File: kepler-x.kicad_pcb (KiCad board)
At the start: 2 copper layers, 140.5 x 150 mm, 7 parts, among them U1 Bus-X68000-ext, U2 74LVT162245, U3 74LVT162245, U4 74LVT162245, U5 CS8421-CZZ, U6 WM8804GEDS/RV

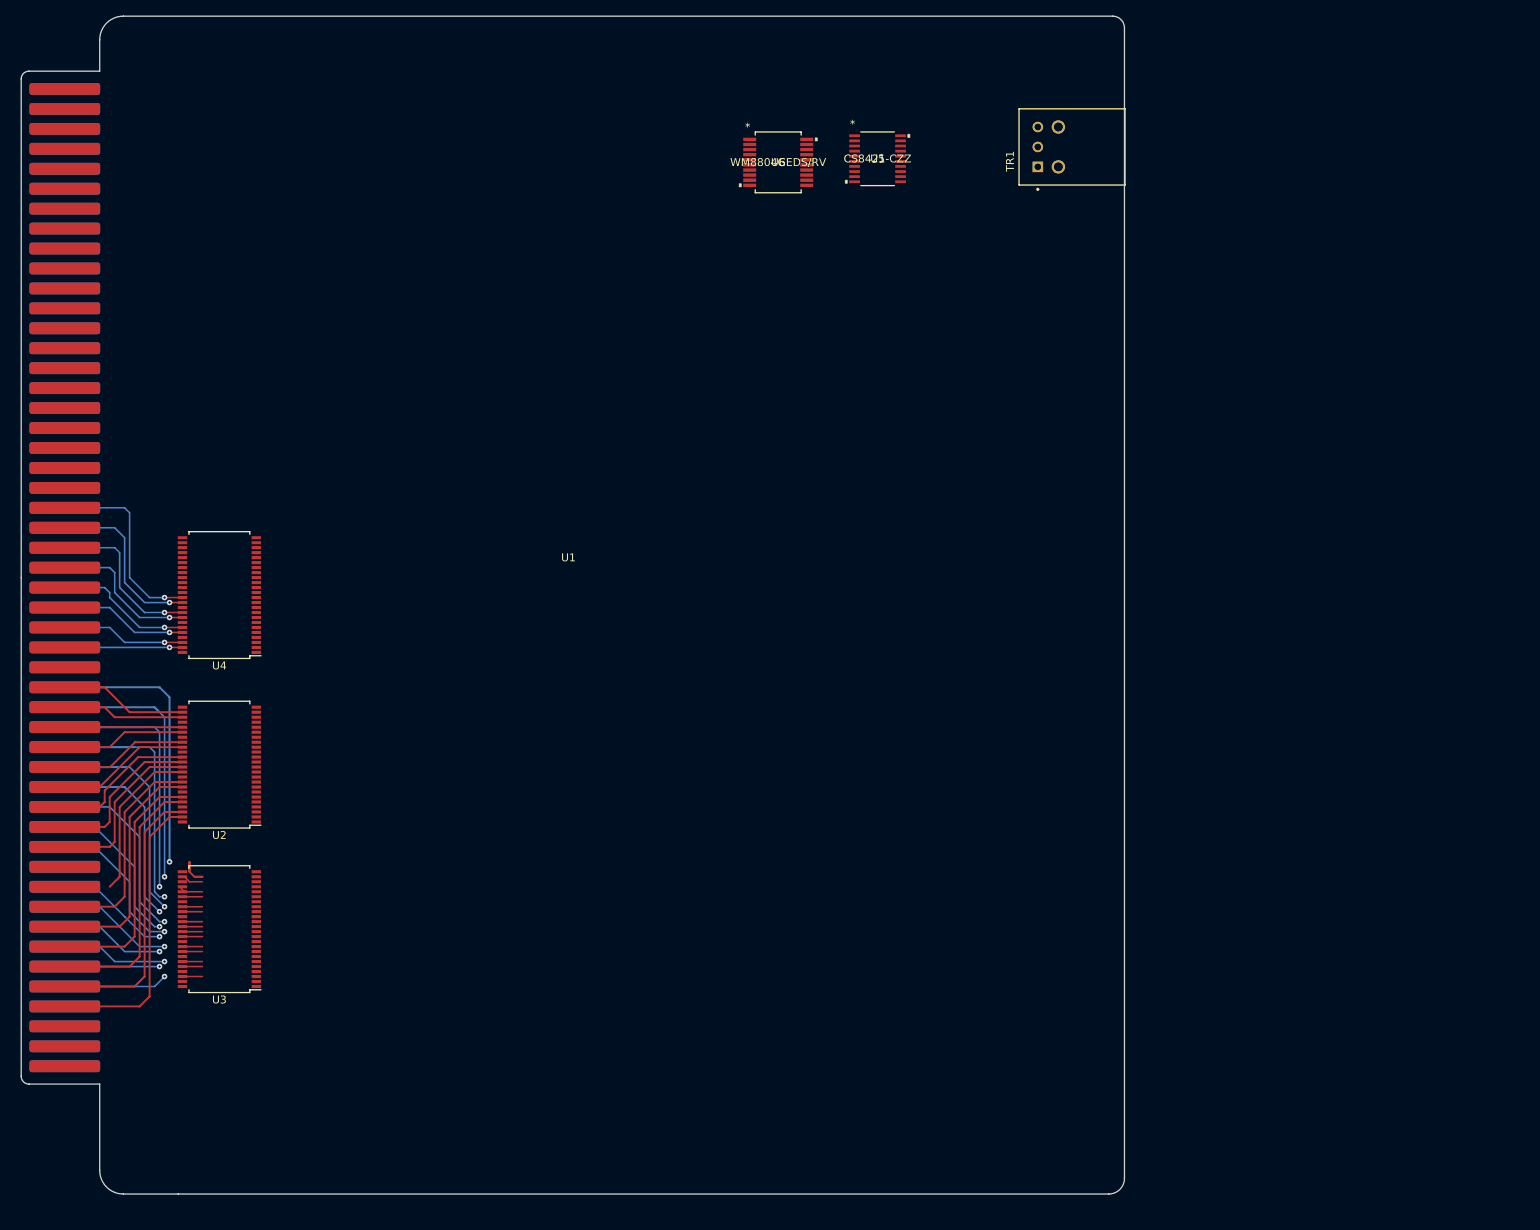
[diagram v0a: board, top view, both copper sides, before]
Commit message: Add fooprints
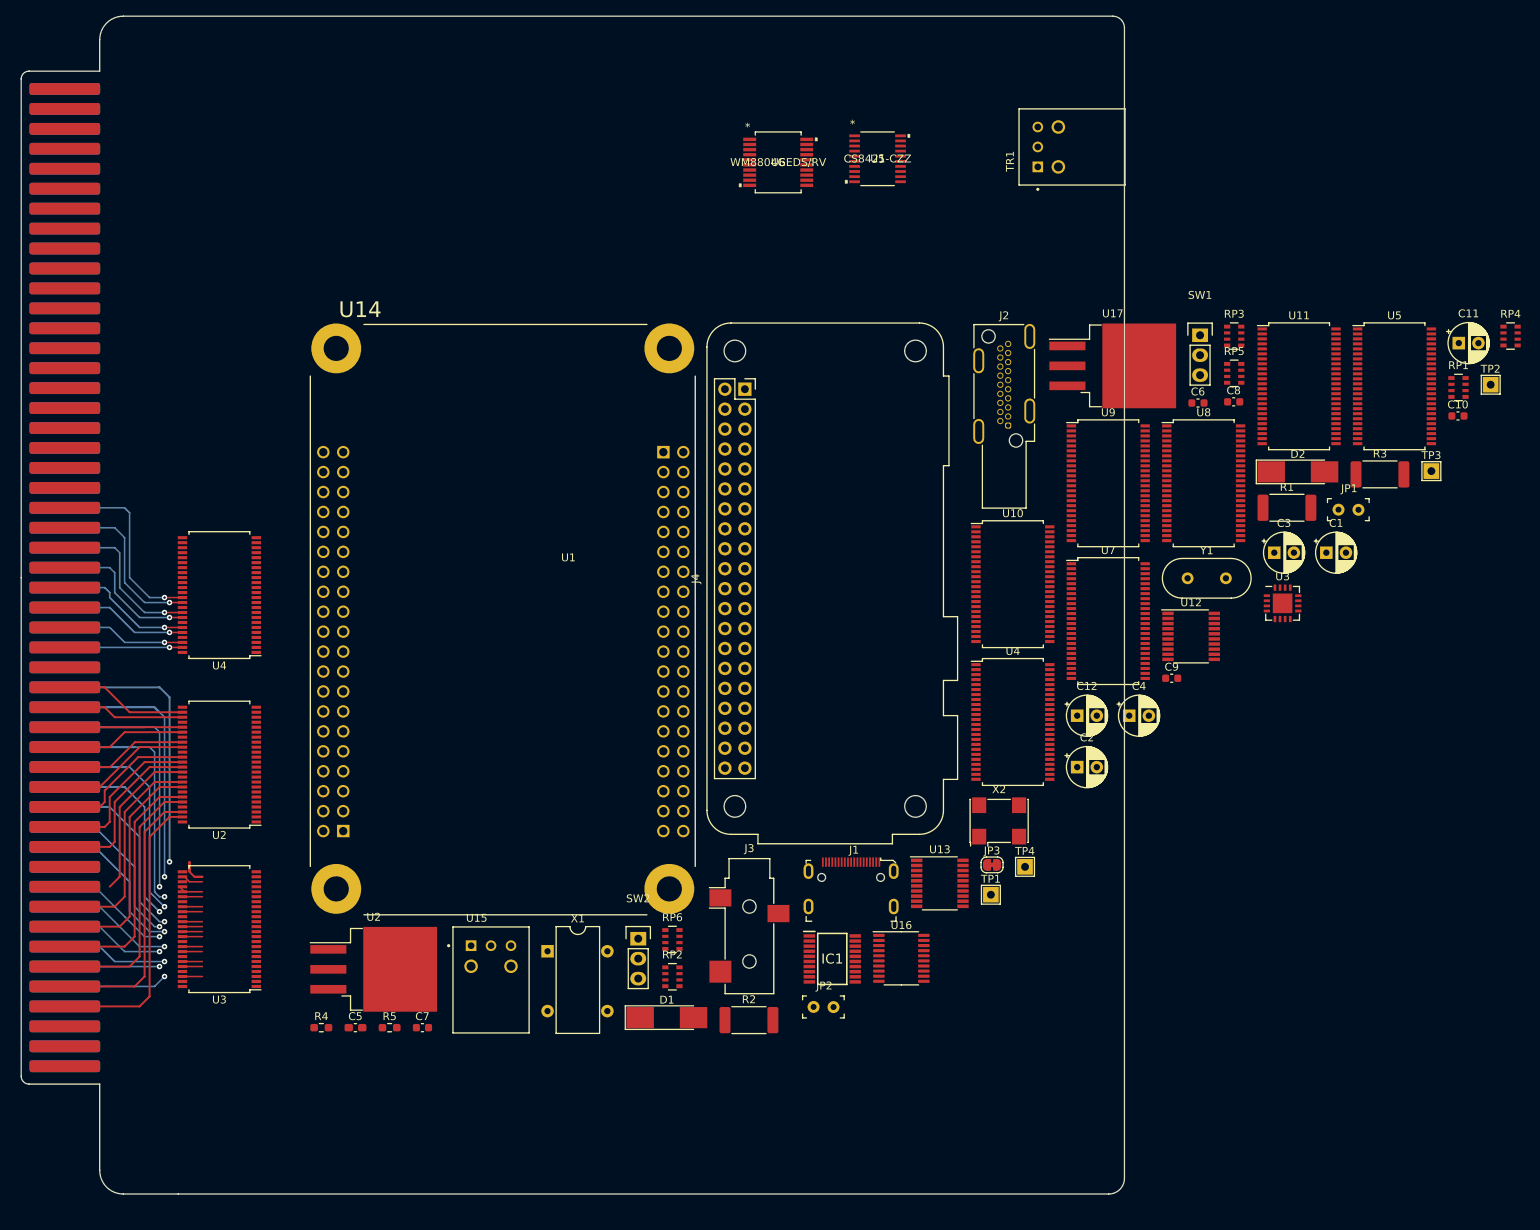
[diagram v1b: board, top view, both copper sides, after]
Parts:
- added C1: 10uF, Capacitor_THT:CP_Radial_D5.0mm_P2.50mm, F.Cu at (196.8, 95.9)
- added C10: 0.1uF, Capacitor_SMD:C_0603_1608Metric, F.Cu at (213.6, 78.5)
- added C11: 10uF, Capacitor_THT:CP_Radial_D5.0mm_P2.50mm, F.Cu at (213.7, 69.2)
- added C12: 100uF, Capacitor_THT:CP_Radial_D5.0mm_P2.50mm, F.Cu at (165.1, 116.6)
- added C2: 100uF, Capacitor_THT:CP_Radial_D5.0mm_P2.50mm, F.Cu at (165.1, 123.2)
- added C3: 1uF, Capacitor_THT:CP_Radial_D5.0mm_P2.50mm, F.Cu at (190.2, 95.9)
- added C4: 15pF, Capacitor_THT:CP_Radial_D5.0mm_P2.50mm, F.Cu at (171.8, 116.6)
- added C5: 15pF, Capacitor_SMD:C_0603_1608Metric_Pad1.08x0.95mm_HandSolder, F.Cu at (73.2, 156.4)
- added C6: 0.1uF, Capacitor_SMD:C_0603_1608Metric, F.Cu at (180.5, 76.8)
- added C7: 0.1uF, Capacitor_SMD:C_0603_1608Metric, F.Cu at (81.7, 156.4)
- added C8: 2.2uF, Capacitor_SMD:C_0603_1608Metric, F.Cu at (185.1, 76.7)
- added C9: 2.2uF, Capacitor_SMD:C_0603_1608Metric, F.Cu at (177.2, 111.9)
- added D1: D_Schottky_Small, Diode_SMD:D_MELF_Handsoldering, F.Cu at (112.9, 155.1)
- added D2: D_Schottky_Small, Diode_SMD:D_MELF_Handsoldering, F.Cu at (193.2, 85.6)
- added IC1: SLG46826G, x68000-ext:SOP65P640X120-20N, F.Cu at (133.9, 147.6)
- added J1: HDMI_C_1.3, digikey-footprints:HDMI_Mini_Female_2001-1-2-21-00-BK, F.Cu at (136.3, 135.3)
- added J2: HDMI_A, Connector_HDMI:HDMI_A_Kycon_KDMIX-SL1-NS-WS-B15_VerticalRightAngle, F.Cu at (156.3, 79.7)
- added J3: Jack_3.5mm_3pin, Connector_Audio:Jack_3.5mm_CUI_SJ-3523-SMT_Horizontal, F.Cu at (123.4, 143.4)
- added J4: RasPI_IO_Header_B+, Module:Raspberry_Pi_Zero_Socketed_THT_FaceDown_MountingHoles, F.Cu at (122.8, 75.1)
- added JP1: Jumper_NC_Small, digikey-footprints:PinHeader_1x2_P2.54mm, F.Cu at (198.4, 90.4)
- added JP2: Jumper_NC_Small, digikey-footprints:PinHeader_1x2_P2.54mm, F.Cu at (131.6, 153.7)
- added JP3: Jumper_NC_Small, Jumper:SolderJumper-2_P1.3mm_Bridged_RoundedPad1.0x1.5mm, F.Cu at (154.3, 135.6)
- added R1: R100 (0.1Ω), Resistor_SMD:R_2512_6332Metric_Pad1.40x3.35mm_HandSolder, F.Cu at (191.8, 90.2)
- added R2: R100 (0.1Ω), Resistor_SMD:R_2512_6332Metric_Pad1.40x3.35mm_HandSolder, F.Cu at (123.3, 155.4)
- added R3: R100 (0.1Ω), Resistor_SMD:R_2512_6332Metric_Pad1.40x3.35mm_HandSolder, F.Cu at (203.7, 85.9)
- added R4: R_US, Resistor_SMD:R_0603_1608Metric_Pad0.98x0.95mm_HandSolder, F.Cu at (68.9, 156.4)
- added R5: R_US, Resistor_SMD:R_0603_1608Metric_Pad0.98x0.95mm_HandSolder, F.Cu at (77.6, 156.4)
- added RP1: R_PACK4, Resistor_SMD:R_Array_Convex_4x0603, F.Cu at (213.7, 74.8)
- added RP2: R_PACK4, Resistor_SMD:R_Array_Convex_4x0603, F.Cu at (113.6, 149.9)
- added RP3: R_PACK4, Resistor_SMD:R_Array_Convex_4x0603, F.Cu at (185.1, 68.3)
- added RP4: R_PACK4, Resistor_SMD:R_Array_Convex_4x0603, F.Cu at (220.3, 68.3)
- added RP5: 270, Resistor_SMD:R_Array_Convex_4x0603, F.Cu at (185.1, 73.0)
- added RP6: 270, Resistor_SMD:R_Array_Convex_4x0603, F.Cu at (113.6, 145.1)
- added SW1: SWITCH_INV, Pin_Headers:Pin_Header_Straight_1x03, F.Cu at (180.8, 68.2)
- added SW2: SWITCH_INV, Pin_Headers:Pin_Header_Straight_1x03, F.Cu at (109.2, 145.0)
- added TP1: TestPoint, TestPoint:TestPoint_THTPad_2.0x2.0mm_Drill1.0mm, F.Cu at (154.1, 139.4)
- added TP2: TestPoint, TestPoint:TestPoint_THTPad_2.0x2.0mm_Drill1.0mm, F.Cu at (217.8, 74.5)
- added TP3: TestPoint, TestPoint:TestPoint_THTPad_2.0x2.0mm_Drill1.0mm, F.Cu at (210.2, 85.5)
- added TP4: TestPoint, TestPoint:TestPoint_THTPad_2.0x2.0mm_Drill1.0mm, F.Cu at (158.5, 135.9)
- added U10: 74AHC16374, Housings_SSOP:SSOP-48_7.5x15.9mm_Pitch0.635mm, F.Cu at (156.9, 99.9)
- added U11: 74LVTH162245, Housings_SSOP:SSOP-48_7.5x15.9mm_Pitch0.635mm, F.Cu at (193.4, 74.7)
- added U12: TC7MPB9307F, Housings_SSOP:TSSOP-20_4.4x6.5mm_Pitch0.65mm, F.Cu at (179.6, 106.5)
- added U13: TC7MPB9307F, Housings_SSOP:TSSOP-20_4.4x6.5mm_Pitch0.65mm, F.Cu at (147.6, 138.0)
- added U14: P0082(DE0-NANO), x68000-ext:MODULE_P0082_BOTTOMMOUNT, F.Cu at (92.0, 104.4)
- added U15: PLR135-T10, x68000-ext:XDCR_PLT133_T10W, F.Cu at (90.5, 148.6)
- added U16: PCM5102, Package_SO:TSSOP-20_4.4x6.5mm_P0.65mm, F.Cu at (142.7, 147.5)
- added U17: LT1117-3.3, Package_TO_SOT_SMD:TO-263-3_TabPin2, F.Cu at (169.7, 72.1)
- added U2: LT1117-3.3, Package_TO_SOT_SMD:TO-263-3_TabPin2, F.Cu at (75.5, 148.9)
- added U3: INA3221, Housings_DFN_QFN:QFN-16-1EP_4x4mm_Pitch0.65mm, F.Cu at (191.3, 102.3)
- added U4: 74AHC16374, Housings_SSOP:SSOP-48_7.5x15.9mm_Pitch0.635mm, F.Cu at (156.9, 117.4)
- added U5: 74AHC16374, Housings_SSOP:SSOP-48_7.5x15.9mm_Pitch0.635mm, F.Cu at (205.5, 74.7)
- added U7: 74AHC16374, Housings_SSOP:SSOP-48_7.5x15.9mm_Pitch0.635mm, F.Cu at (169.1, 104.6)
- added U8: 74AHC16374, Housings_SSOP:SSOP-48_7.5x15.9mm_Pitch0.635mm, F.Cu at (181.2, 87.0)
- added U9: 74AHC16374, Housings_SSOP:SSOP-48_7.5x15.9mm_Pitch0.635mm, F.Cu at (169.1, 87.0)
- added X1: SG-8002DC(24.576MHz), Oscillator:Oscillator_SeikoEpson_SG-8002DC, F.Cu at (97.7, 146.6)
- added X2: ASV-xxxMHz, Oscillator:Oscillator_SMD_Abracon_ASV-4Pin_7.0x5.1mm, F.Cu at (155.2, 130.0)
- added Y1: 12MHz, Crystal:Crystal_HC49-U_Vertical, F.Cu at (179.2, 99.1)
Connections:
- TR1 pad 1: unconnected-(TR1-Pad1) -> Net-(TR1-Pad1)
- TR1 pad 2: unconnected-(TR1-Pad2) -> VCC
- TR1 pad 3: unconnected-(TR1-Pad3) -> GND
- U1 pad A22: unconnected-(U1-PadA22) -> Net-(U1-PadA22)
- U1 pad A23: unconnected-(U1-PadA23) -> Net-(U1-PadA22)
- U1 pad A24: unconnected-(U1-PadA24) -> /ExFC0
- U1 pad A25: unconnected-(U1-PadA25) -> /ExFC1
- U1 pad A26: unconnected-(U1-PadA26) -> /ExFC2
- U1 pad A27: unconnected-(U1-PadA27) -> /ExAS
- U1 pad A28: unconnected-(U1-PadA28) -> /ExLDS
- U1 pad A29: unconnected-(U1-PadA29) -> /ExUDS
- U1 pad A30: unconnected-(U1-PadA30) -> /ExRW
- U1 pad A32: unconnected-(U1-PadA32) -> -12V
- U1 pad A33: unconnected-(U1-PadA33) -> -12V
- U1 pad A36: unconnected-(U1-PadA36) -> /ExDTACK
- U1 pad A37: unconnected-(U1-PadA37) -> /ExEXRESET
- U1 pad A40: unconnected-(U1-PadA40) -> /ExEXPWON
- U1 pad A42: unconnected-(U1-PadA42) -> Net-(U1-PadA42)
- U1 pad A43: unconnected-(U1-PadA43) -> Net-(U1-PadA42)
- U1 pad A49: VCC -> Net-(U1-PadA49)
- U1 pad A50: VCC -> Net-(U1-PadA49)
- U1 pad B2: unconnected-(U1-PadB2) -> /ExCLK10M
- U1 pad B30: unconnected-(U1-PadB30) -> /ExIDDIR
- U1 pad B32: unconnected-(U1-PadB32) -> /ExHSYNC
- U1 pad B33: unconnected-(U1-PadB33) -> /ExVSYNC
- U1 pad B34: unconnected-(U1-PadB34) -> /ExDONE
- U1 pad B35: unconnected-(U1-PadB35) -> /ExDTC
- U1 pad B36: unconnected-(U1-PadB36) -> /ExEXREQ
- U1 pad B37: unconnected-(U1-PadB37) -> /ExEXACK
- U1 pad B38: unconnected-(U1-PadB38) -> /ExEXPCL
- U1 pad B39: unconnected-(U1-PadB39) -> /ExEXOWN
- U1 pad B42: unconnected-(U1-PadB42) -> /ExIRQ2
- U1 pad B43: unconnected-(U1-PadB43) -> /ExIRQ4
- U1 pad B44: unconnected-(U1-PadB44) -> /ExIACK2
- U1 pad B45: unconnected-(U1-PadB45) -> /ExIACK4
- U1 pad B46: unconnected-(U1-PadB46) -> /ExBR
- U1 pad B47: unconnected-(U1-PadB47) -> /ExBG
- U6 pad 10: unconnected-(U6-Pad10) -> Net-(C4-Pad1)
- U6 pad 11: unconnected-(U6-Pad11) -> Net-(C5-Pad1)
- U6 pad 12: unconnected-(U6-Pad12) -> /I2S_DATA_IN
- U6 pad 13: unconnected-(U6-Pad13) -> /I2S_DATA
- U6 pad 14: unconnected-(U6-Pad14) -> /I2S_BCLK
- U6 pad 15: unconnected-(U6-Pad15) -> /I2S_LRCK
- U6 pad 16: unconnected-(U6-Pad16) -> /I2S_MCLK
- U6 pad 17: unconnected-(U6-Pad17) -> Net-(TR1-Pad1)
- U6 pad 18: unconnected-(U6-Pad18) -> GND
- U6 pad 19: unconnected-(U6-Pad19) -> +3V3
- U6 pad 20: unconnected-(U6-Pad20) -> Net-(U15-Pad3)
- U6 pad 7: unconnected-(U6-Pad7) -> +3V3
- U6 pad 8: unconnected-(U6-Pad8) -> GND
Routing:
- net /ExAB15: track 45.0 -> 42.5 mm
- net /ExAB14: track 37.0 -> 39.5 mm

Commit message: Today's version
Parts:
- removed J2: HDMI_A, Connector_HDMI:HDMI_A_Kycon_KDMIX-SL1-NS-WS-B15_VerticalRightAngle
- removed the U2 at (55.9, 122.9)
- removed the U3 at (191.3, 102.3)
- removed the U4 at (156.9, 117.4)
- removed the U5 at (205.5, 74.7)
- added H1: MountingHole, MountingHole:MountingHole_3.7mm, F.Cu at (166.0, 173.0)
- added H2: MountingHole, MountingHole:MountingHole_3.7mm, F.Cu at (166.0, 37.0)
- added H3: MountingHole, MountingHole:MountingHole_2.7mm_M2.5, F.Cu at (152.5, 174.0)
- added H4: MountingHole, MountingHole:MountingHole_2.7mm_M2.5, F.Cu at (152.5, 108.0)
- added J5: Jack_3.5mm_3pin, Connector_Audio:Jack_3.5mm_Switronic_ST-005-G_horizontal, F.Cu at (164.5, 97.8)
- added J6: Jack_3.5mm_3pin, Connector_Audio:Jack_3.5mm_Switronic_ST-005-G_horizontal, F.Cu at (164.5, 107.3)
- C10, C6: footprint Capacitor_SMD:C_0603_1608Metric -> Capacitor_SMD:C_0603_1608Metric_Pad1.08x0.95mm_HandSolder
- C3, C4: footprint Capacitor_THT:CP_Radial_D5.0mm_P2.50mm -> Capacitor_SMD:C_0603_1608Metric_Pad1.08x0.95mm_HandSolder
- C7, C8, C9: footprint Capacitor_SMD:C_0603_1608Metric -> Capacitor_SMD:C_0603_1608Metric_Pad1.08x0.95mm_HandSolder; moved to B.Cu
- J3: footprint Connector_Audio:Jack_3.5mm_CUI_SJ-3523-SMT_Horizontal -> Connector_Audio:Jack_3.5mm_Switronic_ST-005-G_horizontal
- R1, R2, R3, U10, U11, U16, U17, U2, U8, U9, X2: moved to B.Cu
- U3: value 74LVT162245 -> INA3221; footprint Housings_SSOP:SSOP-48_7.5x15.9mm_Pitch0.635mm -> Housings_DFN_QFN:QFN-16-1EP_4x4mm_Pitch0.65mm; moved to B.Cu
- U4: value 74LVT162245 -> 74AHC16374
- U5: value CS8421-CZZ -> 74AHC16374; footprint x68000-ext:CS8421-CZZ -> Housings_SSOP:SSOP-48_7.5x15.9mm_Pitch0.635mm
- moved RP4 165.7 mm to (55.2, 82.5)
- moved R3 158.8 mm to (52.1, 38.7), turned to 180 degrees
- moved RP1 158.6 mm to (55.2, 67.3)
- moved R1 150.5 mm to (52.1, 34.3), turned to 180 degrees
- moved C1 146.0 mm to (57.8, 51.4), turned to 90 degrees
- moved U11 143.2 mm to (50.2, 73.7)
- moved SW1 136.8 mm to (44.4, 57.1), turned to 90 degrees
- moved U12 136.6 mm to (48.3, 69.2), turned to 180 degrees
- moved R2 132.9 mm to (52.1, 43.2), turned to 180 degrees
- moved RP3 129.9 mm to (55.2, 71.1)
- moved R4 127.0 mm to (158.1, 66.0), turned to 180 degrees
- moved C2 126.8 mm to (56.5, 57.8)
- moved U8 125.0 mm to (57.8, 106.7)
- moved C7 121.4 mm to (130.2, 45.1), turned to 90 degrees
- moved R5 119.6 mm to (158.1, 67.9), turned to 180 degrees
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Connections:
- R1 pad 1: Net-(U1-PadA49) -> Net-(R1-Pad1)
- R2 pad 1: Net-(U1-PadA22) -> Net-(R2-Pad1)
- R3 pad 1: Net-(U1-PadA42) -> Net-(R3-Pad1)
- R3 pad 2: Net-(TP1-Pad1) -> Net-(R3-Pad2)
- TP1 pad 1: Net-(TP1-Pad1) -> Net-(R3-Pad2)
- U1 pad A22: Net-(U1-PadA22) -> Net-(R2-Pad1)
- U1 pad A23: Net-(U1-PadA22) -> Net-(R2-Pad1)
- U1 pad A42: Net-(U1-PadA42) -> Net-(R3-Pad1)
- U1 pad A43: Net-(U1-PadA42) -> Net-(R3-Pad1)
- U1 pad A49: Net-(U1-PadA49) -> Net-(R1-Pad1)
- U1 pad A50: Net-(U1-PadA49) -> Net-(R1-Pad1)
- U10 pad 11: /ExDB9 -> /ExDB6
- U10 pad 12: /ExDB8 -> /ExDB7
- U10 pad 13: /ExDB7 -> /ExDB8
- U10 pad 14: /ExDB6 -> /ExDB9
- U10 pad 16: /ExDB5 -> /ExDB10
- U10 pad 17: /ExDB4 -> /ExDB11
- U10 pad 19: /ExDB3 -> /ExDB12
- U10 pad 2: /ExDB15 -> /ExDB0
- U10 pad 20: /ExDB2 -> /ExDB13
- U10 pad 22: /ExDB1 -> /ExDB14
- U10 pad 23: /ExDB0 -> /ExDB15
- U10 pad 26: /iSB0 -> /iSB15
- U10 pad 27: /iSB1 -> /iSB14
- U10 pad 29: /iSB2 -> /iSB13
- U10 pad 3: /ExDB14 -> /ExDB1
- U10 pad 30: /iSB3 -> /iSB12
- U10 pad 32: /iSB4 -> /iSB11
- U10 pad 33: /iSB5 -> /iSB10
- U10 pad 35: /iSB6 -> /iSB9
- U10 pad 36: /iSB7 -> /iSB8
- U10 pad 37: /iSB8 -> /iSB7
- U10 pad 38: /iSB9 -> /iSB6
- U10 pad 40: /iSB10 -> /iSB5
- U10 pad 41: /iSB11 -> /iSB4
- U10 pad 43: /iSB12 -> /iSB3
- U10 pad 44: /iSB13 -> /iSB2
- U10 pad 46: /iSB14 -> /iSB1
- U10 pad 47: /iSB15 -> /iSB0
- U10 pad 5: /ExDB13 -> /ExDB2
- U10 pad 6: /ExDB12 -> /ExDB3
- U10 pad 8: /ExDB11 -> /ExDB4
- U10 pad 9: /ExDB10 -> /ExDB5
- U3 pad 1: unconnected-(U3-Pad1) -> Net-(R3-Pad2)
- U3 pad 11: unconnected-(U3-Pad11) -> VCC
- U3 pad 12: unconnected-(U3-Pad12) -> Net-(R1-Pad1)
- U3 pad 14: unconnected-(U3-Pad14) -> +12V
- U3 pad 15: unconnected-(U3-Pad15) -> Net-(R2-Pad1)
- U3 pad 17: unconnected-(U3-Pad17) -> (no net)
- U3 pad 2: unconnected-(U3-Pad2) -> Net-(R3-Pad1)
- U3 pad 3: unconnected-(U3-Pad3) -> GND
- U3 pad 4: unconnected-(U3-Pad4) -> VCC
- U4 pad 1: unconnected-(U4-Pad1) -> /iB_AI_OE_U
- U4 pad 10: unconnected-(U4-Pad10) -> GND
- U4 pad 11: unconnected-(U4-Pad11) -> /iSB6
- U4 pad 12: unconnected-(U4-Pad12) -> /iSB7
- U4 pad 13: unconnected-(U4-Pad13) -> /iSB8
- U4 pad 14: unconnected-(U4-Pad14) -> /iSB9
- U4 pad 15: unconnected-(U4-Pad15) -> GND
- U4 pad 16: unconnected-(U4-Pad16) -> /iSB10
- U4 pad 17: unconnected-(U4-Pad17) -> /iSB11
- U4 pad 19: unconnected-(U4-Pad19) -> /iSB12
- U4 pad 2: unconnected-(U4-Pad2) -> /iSB0
- U4 pad 20: unconnected-(U4-Pad20) -> /iSB13
- U4 pad 21: unconnected-(U4-Pad21) -> GND
- U4 pad 22: unconnected-(U4-Pad22) -> /iSB14
- U4 pad 23: unconnected-(U4-Pad23) -> /iSB15
- U4 pad 24: unconnected-(U4-Pad24) -> /iB_AI_OE_U
- U4 pad 25: unconnected-(U4-Pad25) -> /iB_AI_CK
- U4 pad 28: unconnected-(U4-Pad28) -> GND
- U4 pad 3: unconnected-(U4-Pad3) -> /iSB1
- U4 pad 33: unconnected-(U4-Pad33) -> /ExFC2
- U4 pad 34: unconnected-(U4-Pad34) -> GND
- U4 pad 35: unconnected-(U4-Pad35) -> /ExFC1
- U4 pad 36: unconnected-(U4-Pad36) -> /ExFC0
- U4 pad 39: unconnected-(U4-Pad39) -> GND
- U4 pad 4: unconnected-(U4-Pad4) -> GND
- U4 pad 42: unconnected-(U4-Pad42) -> +3V3
- U4 pad 45: unconnected-(U4-Pad45) -> GND
- U4 pad 48: unconnected-(U4-Pad48) -> /iB_AI_CK
- U4 pad 5: unconnected-(U4-Pad5) -> /iSB2
- U4 pad 6: unconnected-(U4-Pad6) -> /iSB3
- U4 pad 7: unconnected-(U4-Pad7) -> +3V3
- U4 pad 8: unconnected-(U4-Pad8) -> /iSB4
- U4 pad 9: unconnected-(U4-Pad9) -> /iSB5
- U5 pad 1: unconnected-(U5-Pad1) -> /iB_AI_OE_L
- U5 pad 10: unconnected-(U5-Pad10) -> GND
- U5 pad 11: unconnected-(U5-Pad11) -> /iSB6
- U5 pad 12: unconnected-(U5-Pad12) -> /iSB7
- U5 pad 13: unconnected-(U5-Pad13) -> /iSB8
- U5 pad 14: unconnected-(U5-Pad14) -> /iSB9
- U5 pad 15: unconnected-(U5-Pad15) -> GND
- U5 pad 16: unconnected-(U5-Pad16) -> /iSB10
- U5 pad 17: unconnected-(U5-Pad17) -> /iSB11
- U5 pad 18: unconnected-(U5-Pad18) -> (no net)
- U5 pad 19: unconnected-(U5-Pad19) -> /iSB12
- U5 pad 2: unconnected-(U5-Pad2) -> /iSB0
- U5 pad 20: unconnected-(U5-Pad20) -> /iSB13
- U5 pad 3: unconnected-(U5-Pad3) -> /iSB1
- U5 pad 4: unconnected-(U5-Pad4) -> GND
- U5 pad 5: unconnected-(U5-Pad5) -> /iSB2
- U5 pad 6: unconnected-(U5-Pad6) -> /iSB3
- U5 pad 7: unconnected-(U5-Pad7) -> +3V3
- U5 pad 8: unconnected-(U5-Pad8) -> /iSB4
- U5 pad 9: unconnected-(U5-Pad9) -> /iSB5
- U8 pad 11: /ExFC1 -> /ExAB22
- U8 pad 12: /ExFC0 -> /ExAB23
- U8 pad 13: /ExAB23 -> /ExFC0
- U8 pad 14: /ExAB22 -> /ExFC1
- U8 pad 16: /ExAB21 -> /ExFC2
- U8 pad 17: /ExAB20 -> unconnected-(U8-Pad17)
- U8 pad 19: /ExAB19 -> unconnected-(U8-Pad19)
- U8 pad 2: unconnected-(U8-Pad2) -> /ExAB16
- U8 pad 20: /ExAB18 -> unconnected-(U8-Pad20)
- U8 pad 22: /ExAB17 -> unconnected-(U8-Pad22)
- U8 pad 23: /ExAB16 -> unconnected-(U8-Pad23)
- U8 pad 26: /iSB0 -> /iSB15
- U8 pad 27: /iSB1 -> /iSB14
- U8 pad 29: /iSB2 -> /iSB13
- U8 pad 3: unconnected-(U8-Pad3) -> /ExAB17
- U8 pad 30: /iSB3 -> /iSB12
- U8 pad 32: /iSB4 -> /iSB11
- U8 pad 33: /iSB5 -> /iSB10
- U8 pad 35: /iSB6 -> /iSB9
- U8 pad 36: /iSB7 -> /iSB8
- U8 pad 37: /iSB8 -> /iSB7
- U8 pad 38: /iSB9 -> /iSB6
- U8 pad 40: /iSB10 -> /iSB5
- U8 pad 41: /iSB11 -> /iSB4
- U8 pad 43: /iSB12 -> /iSB3
- U8 pad 44: /iSB13 -> /iSB2
- U8 pad 46: /iSB14 -> /iSB1
- U8 pad 47: /iSB15 -> /iSB0
- U8 pad 5: unconnected-(U8-Pad5) -> /ExAB18
- U8 pad 6: unconnected-(U8-Pad6) -> /ExAB19
- U8 pad 8: unconnected-(U8-Pad8) -> /ExAB20
- U8 pad 9: /ExFC2 -> /ExAB21
- U9 pad 1: /iB_AO_OE -> unconnected-(U9-Pad1)
- U9 pad 11: /ExAB9 -> /ExAB6
- U9 pad 12: /ExAB8 -> /ExAB7
- U9 pad 13: /ExAB7 -> /ExAB8
- U9 pad 14: /ExAB6 -> /ExAB9
- U9 pad 16: /ExAB5 -> /ExAB10
- U9 pad 17: /ExAB4 -> /ExAB11
- U9 pad 19: /ExAB3 -> /ExAB12
- U9 pad 2: /ExAB15 -> unconnected-(U9-Pad2)
- U9 pad 20: /ExAB2 -> /ExAB13
- U9 pad 22: /ExAB1 -> /ExAB14
- U9 pad 23: unconnected-(U9-Pad23) -> /ExAB15
- U9 pad 26: /iSB0 -> /iSB15
- U9 pad 27: /iSB1 -> /iSB14
- U9 pad 29: /iSB2 -> /iSB13
- U9 pad 3: /ExAB14 -> /ExAB1
- U9 pad 30: /iSB3 -> /iSB12
- U9 pad 32: /iSB4 -> /iSB11
- U9 pad 33: /iSB5 -> /iSB10
- U9 pad 35: /iSB6 -> /iSB9
- U9 pad 36: /iSB7 -> /iSB8
- U9 pad 37: /iSB8 -> /iSB7
- U9 pad 38: /iSB9 -> /iSB6
- U9 pad 40: /iSB10 -> /iSB5
- U9 pad 41: /iSB11 -> /iSB4
- U9 pad 43: /iSB12 -> /iSB3
- U9 pad 44: /iSB13 -> /iSB2
- U9 pad 46: /iSB14 -> /iSB1
- U9 pad 47: /iSB15 -> /iSB0
- U9 pad 5: /ExAB13 -> /ExAB2
- U9 pad 6: /ExAB12 -> /ExAB3
- U9 pad 8: /ExAB11 -> /ExAB4
- U9 pad 9: /ExAB10 -> /ExAB5
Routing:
- net GND: track 0.00 -> 64.5 mm, vias 0 -> 2
- net /ExDB0: track 36.9 -> 0.00 mm
- net /ExIDDIR: track 0.00 -> 24.6 mm, vias 0 -> 1
- net /ExDB7: track 22.2 -> 0.00 mm
- net /ExDB13: track 15.4 -> 36.3 mm
- net /ExAB7: track 17.9 -> 0.00 mm, vias 1 -> 0
- net /ExAB1: track 18.1 -> 2.28 mm, vias 1 -> 0
- net /ExAB16: track 15.0 -> 0.00 mm, vias 1 -> 0
- net /ExAB6: track 13.8 -> 0.00 mm, vias 1 -> 0
- net /ExAB3: track 11.3 -> 23.4 mm, vias 1 -> 2
- net /ExAB9: track 28.4 -> 16.5 mm
- net /ExDB6: track 20.5 -> 27.9 mm
- net /ExAB15: track 42.5 -> 37.0 mm
- net /iB_DI_CK: track 0.00 -> 5.14 mm
- net /ExAB8: track 19.4 -> 15.6 mm
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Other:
- copper layers 2 -> 4
